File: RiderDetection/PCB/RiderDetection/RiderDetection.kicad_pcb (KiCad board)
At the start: 2 copper layers, 16 parts, among them J1 Conn_01x19, J2 Conn_01x19, J3 Conn_01x06, J4 Conn_01x03_Male, J5 Conn_01x03_Male, K1 G5V-1, K2 G5V-1, K3 G5V-1, U1 ULN2003A

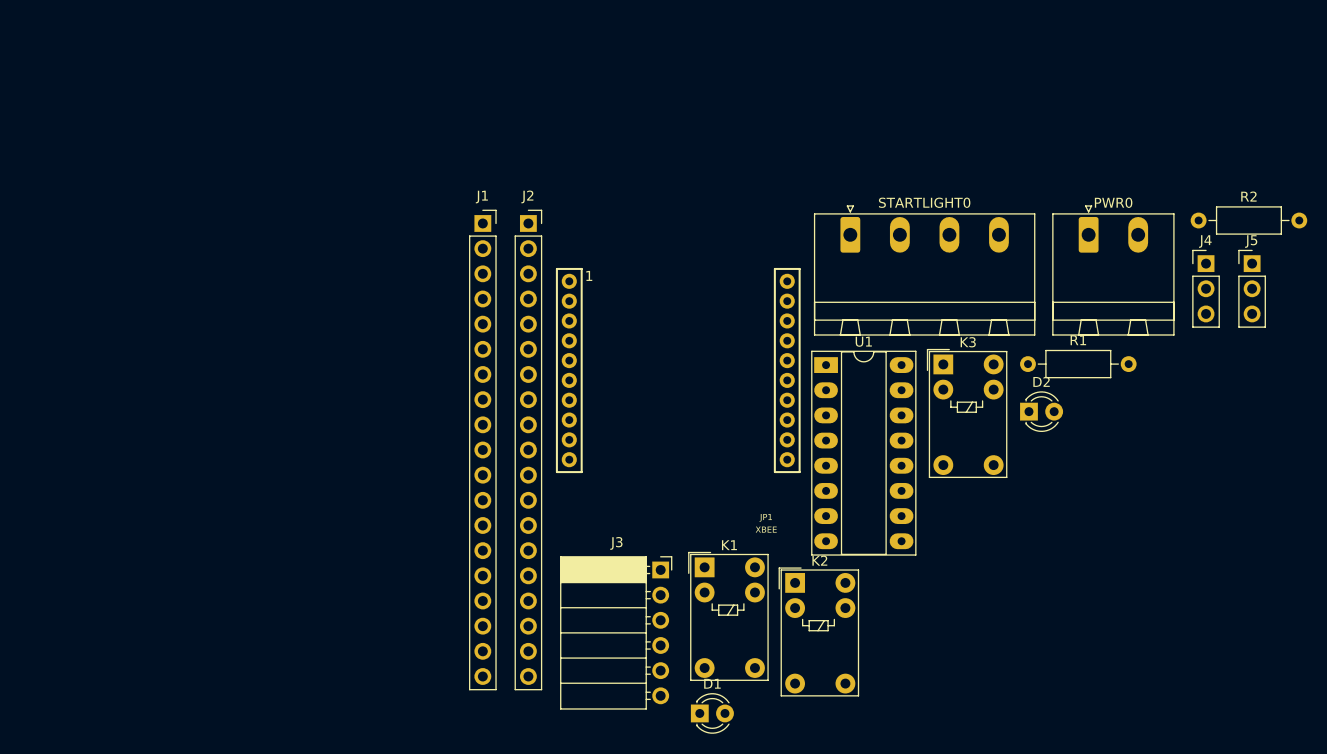
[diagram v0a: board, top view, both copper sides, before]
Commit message: Issue 19: Carrier PCB for rider ID
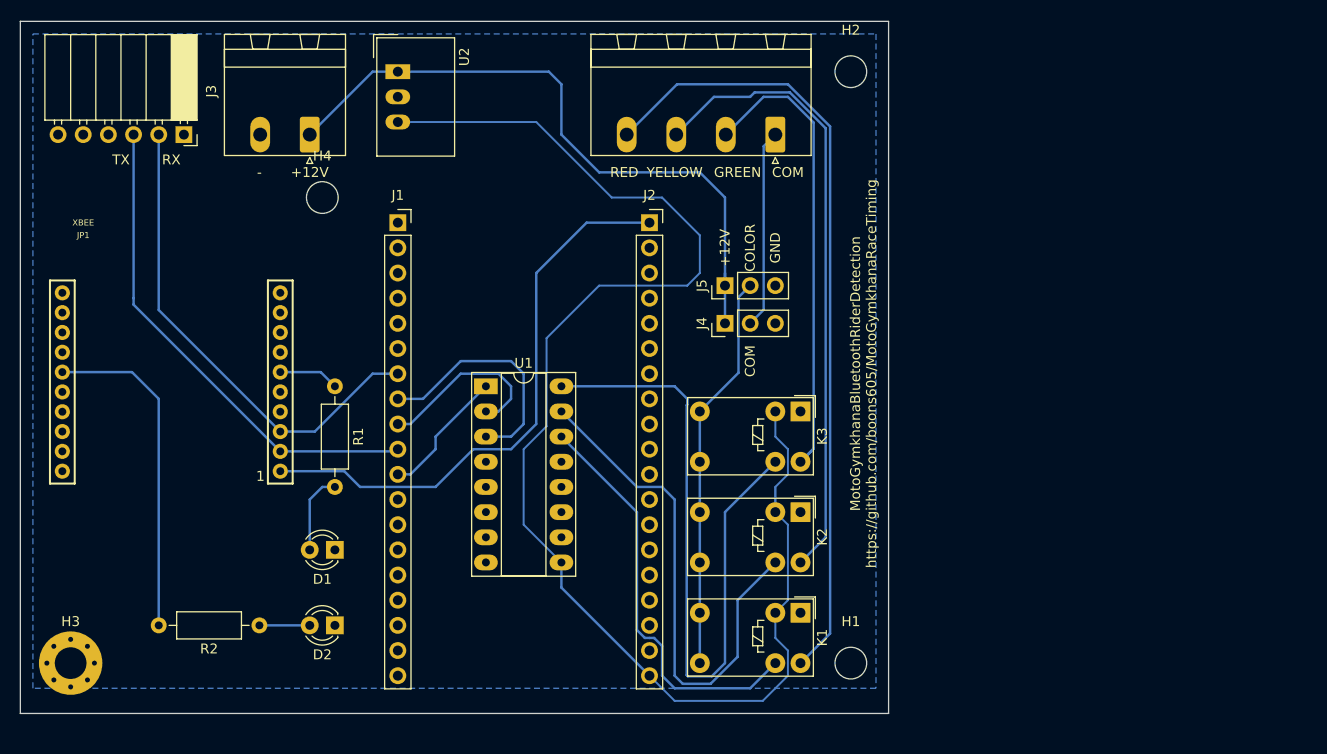
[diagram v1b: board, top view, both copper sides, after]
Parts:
- added H1: MountingHole, MountingHole:MountingHole_3.2mm_M3, F.Cu at (133.3, 113.0)
- added H2: MountingHole, MountingHole:MountingHole_3.2mm_M3, F.Cu at (133.3, 53.3)
- added H3: MountingHole_Pad, MountingHole:MountingHole_3.2mm_M3_Pad_Via, F.Cu at (54.6, 113.0)
- added H4: MountingHole, MountingHole:MountingHole_3.2mm_M3, F.Cu at (80.0, 66.0)
- added U2: TSR_1-2450, Converter_DCDC:Converter_DCDC_TRACO_TSR-1_THT, F.Cu at (87.6, 53.3)
- K1, K2, K3: footprint Relay_THT:Relay_SPDT_Omron_G5V-1 -> RiderDetection:Relay_SPDT_Omron_G5V-1
- moved R2 103.2 mm to (73.7, 109.2), turned to 180 degrees
- moved PWR0 79.3 mm to (78.7, 59.7), turned to 180 degrees
- moved D2 73.3 mm to (81.3, 109.2), turned to 180 degrees
- moved R1 70.0 mm to (81.3, 85.1), turned to 270 degrees
- moved J3 65.2 mm to (66.0, 59.7), turned to 270 degrees
- moved JP1 55.2 mm to (64.8, 73.7), turned to 180 degrees
- moved J5 53.2 mm to (120.7, 74.9), turned to 90 degrees
- moved J4 48.9 mm to (120.7, 78.7), turned to 90 degrees
- moved D1 40.4 mm to (81.3, 101.6), turned to 180 degrees
- moved U1 34.4 mm to (96.5, 85.1)
- moved K3 15.2 mm to (128.3, 87.6), turned to 270 degrees
- moved STARTLIGHT0 12.6 mm to (125.7, 59.7), turned to 180 degrees
- moved J2 12.2 mm to (113.0, 68.6)
- moved K1 10.7 mm to (128.3, 108.0), turned to 270 degrees
- moved J1 8.58 mm to (87.6, 68.6)
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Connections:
- U1 pad 14: Net-(K3-Pad9) -> Net-(K1-Pad9)
- U1 pad 16: Net-(K1-Pad9) -> Net-(K3-Pad9)
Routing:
- net +5V: track 0.00 -> 142.9 mm
- net COL_RD: track 0.00 -> 79.8 mm
- net Net-(K3-Pad9): track 0.00 -> 68.0 mm
- net +12V: track 0.00 -> 66.7 mm
- net COL_YW: track 0.00 -> 63.2 mm
- net +3V3: track 0.00 -> 57.9 mm
- net Net-(K2-Pad9): track 0.00 -> 51.8 mm
- net TXD: track 0.00 -> 50.1 mm
- net RXD: track 0.00 -> 49.7 mm
- net COL_GRN: track 0.00 -> 48.1 mm
- net Net-(K1-Pad9): track 0.00 -> 41.9 mm
- net START_COLOR_COM: track 0.00 -> 40.2 mm
- net Net-(JP1-Pad15): track 0.00 -> 33.7 mm
- net Net-(J1-Pad8): track 0.00 -> 24.2 mm
- net START_COM: track 0.00 -> 20.1 mm
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- added copper zone on B.Cu, net GND
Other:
- board outline added: 87.6 x 69.8 mm
- net class Thin added: clearance 0.15, trace_width 0.2, via_dia 0.8, via_drill 0.4
- board text added: "+12V"
- board text added: "-"
- board text added: "COLOR"
- board text added: "COM"
- board text added: "GND"
- board text added: "GREEN"
- board text added: "MotoGymkhanaBluetoothRiderDetection https://github.com/boons605/MotoGymkhanaRaceTiming"
- board text added: "RED"
- board text added: "RX"
- board text added: "TX"
- board text added: "YELLOW"
